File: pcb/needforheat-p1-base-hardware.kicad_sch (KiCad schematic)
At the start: 18 parts, among them IC1 74HC14D,653, J1 Conn_02x08_Counter_Clockwise, J2 RJ12, J3 RJ12, Q1 MMBT3904, Q2 MMBT5401, SW1 DSHP03TSGER, U1 SFH6206-2T

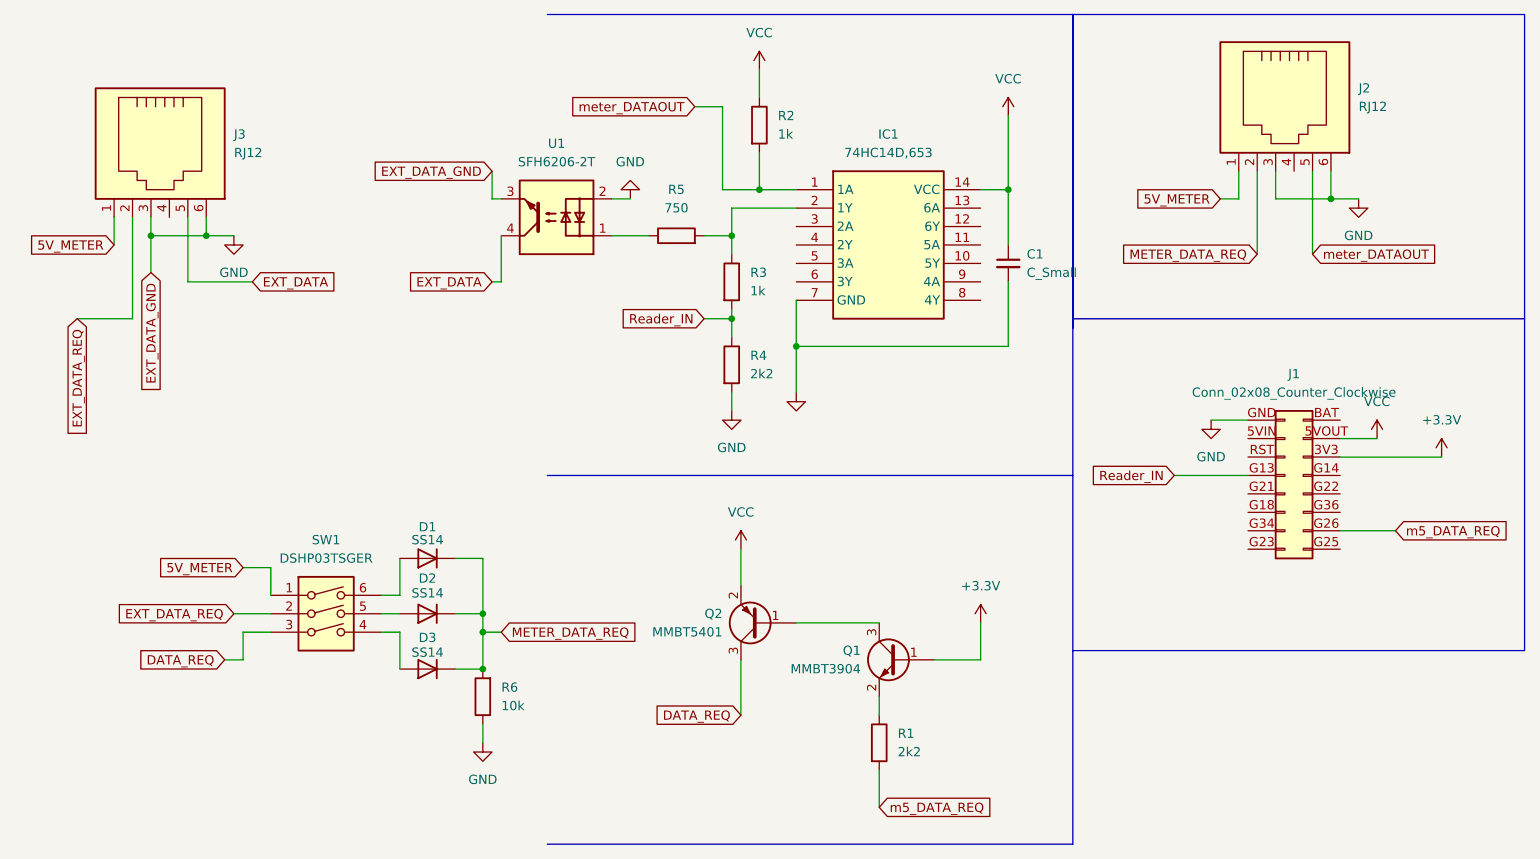
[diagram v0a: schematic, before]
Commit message: updated the pcb files to p1-base v2.4
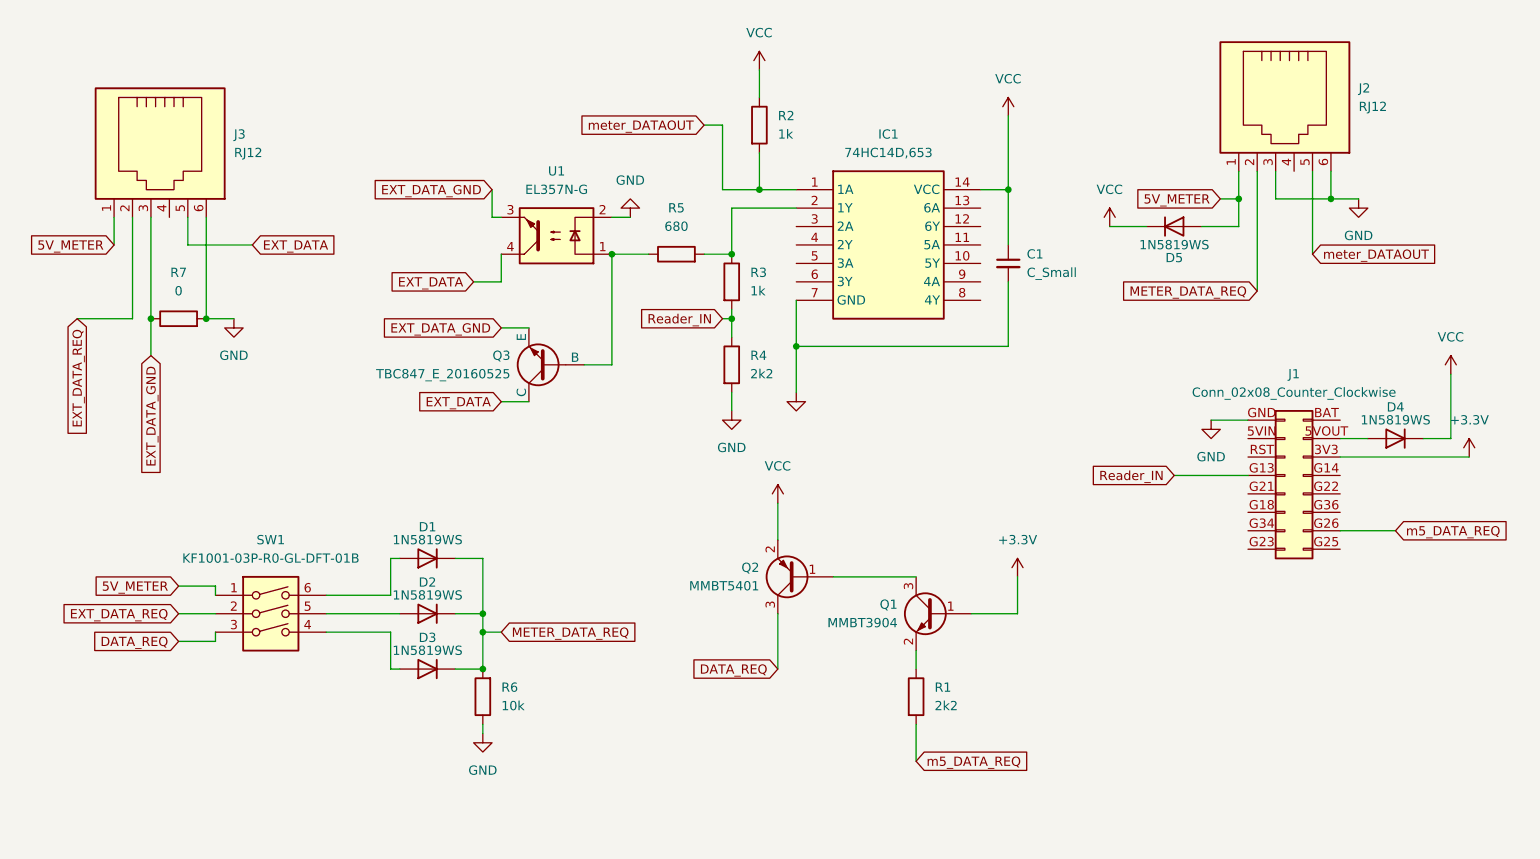
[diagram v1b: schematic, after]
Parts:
- removed U1: SFH6206-2T, Package_DIP:SMDIP-4_W9.53mm_Clearance8mm, symbol Isolator:SFH6206-2T
- added D4, D5: 1N5819WS, Diode_SMD:D_SOD-323, symbol Diode:1N4148WT
- added Q3: TBC847_E_20160525, Package_TO_SOT_SMD:SOT-23-3, symbol Simulation_SPICE:NPN
- added R7: 0, Resistor_SMD:R_0805_2012Metric, symbol Device:R
- added U1: EL357N-G, Package_SO:SOP-4_3.8x4.1mm_P2.54mm, symbol Isolator:EL817
- D1, D2, D3: value SS14 -> 1N5819WS; footprint Diode_SMD:D_SOD-523 -> Diode_SMD:D_SOD-323
- R5: value 750 -> 680
- SW1: value DSHP03TSGER -> KF1001-03P-R0-GL-DFT-01B; footprint Package_DIP:SMDIP-6_W7.62mm -> Package_DIP:DIP-6_W7.62mm_Socket
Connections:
- net 5V_METER: now also D5.2 (A)
- net EXT_DATA: now also Q3.1 (C), U1.4
- net GND: now also R7.2, U1.2; no longer J3.3
- net VCC: now also D4.1 (K), D5.1 (K); no longer J1.5VOUT (Pin_15)
- net at R5.1: now also Q3.2 (B), U1.1
- new net: D4.2 (A), J1.5VOUT (Pin_15)
- new net EXT_DATA_GND: J3.3, Q3.3 (E), R7.1, U1.3
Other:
- moved on the sheet: Q1, Q2, R1, R5, SW1
